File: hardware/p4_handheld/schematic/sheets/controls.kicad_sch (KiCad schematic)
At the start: 0 parts

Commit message: hw(p4_handheld): controls sheet, 11 direct-GPIO buttons off strap pins
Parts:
- added SW1: NavSwitch-Up, SW-SMD_4P-L4.5-W4.5-P3.00-LS4.5-TL, symbol Switch:SW_Push
- added SW10A: Btn-VolUp, SW-SMD_2P-L3.9-W2.9-P1.90-LS2.8-BR, symbol Switch:SW_Push
- added SW10B: Btn-VolDown, SW-SMD_2P-L3.9-W2.9-P1.90-LS2.8-BR, symbol Switch:SW_Push
- added SW11: NavSwitch-Center, SW-SMD_4P-L4.5-W4.5-P3.00-LS4.5-TL, symbol Switch:SW_Push
- added SW2: NavSwitch-Down, SW-SMD_4P-L4.5-W4.5-P3.00-LS4.5-TL, symbol Switch:SW_Push
- added SW3: NavSwitch-Left, SW-SMD_4P-L4.5-W4.5-P3.00-LS4.5-TL, symbol Switch:SW_Push
- added SW4: NavSwitch-Right, SW-SMD_4P-L4.5-W4.5-P3.00-LS4.5-TL, symbol Switch:SW_Push
- added SW5: Btn-Undo, SW-SMD_4P-L6.0-W6.0-P4.50-LS6.5-TL, symbol Switch:SW_Push
- added SW6: Btn-Action, SW-SMD_4P-L6.0-W6.0-P4.50-LS6.5-TL, symbol Switch:SW_Push
- added SW7: Btn-Restart, SW-SMD_4P-L6.0-W6.0-P4.50-LS6.5-TL, symbol Switch:SW_Push
- added SW8: Btn-Menu, SW-SMD_4P-L6.0-W6.0-P4.50-LS6.5-TL, symbol Switch:SW_Push

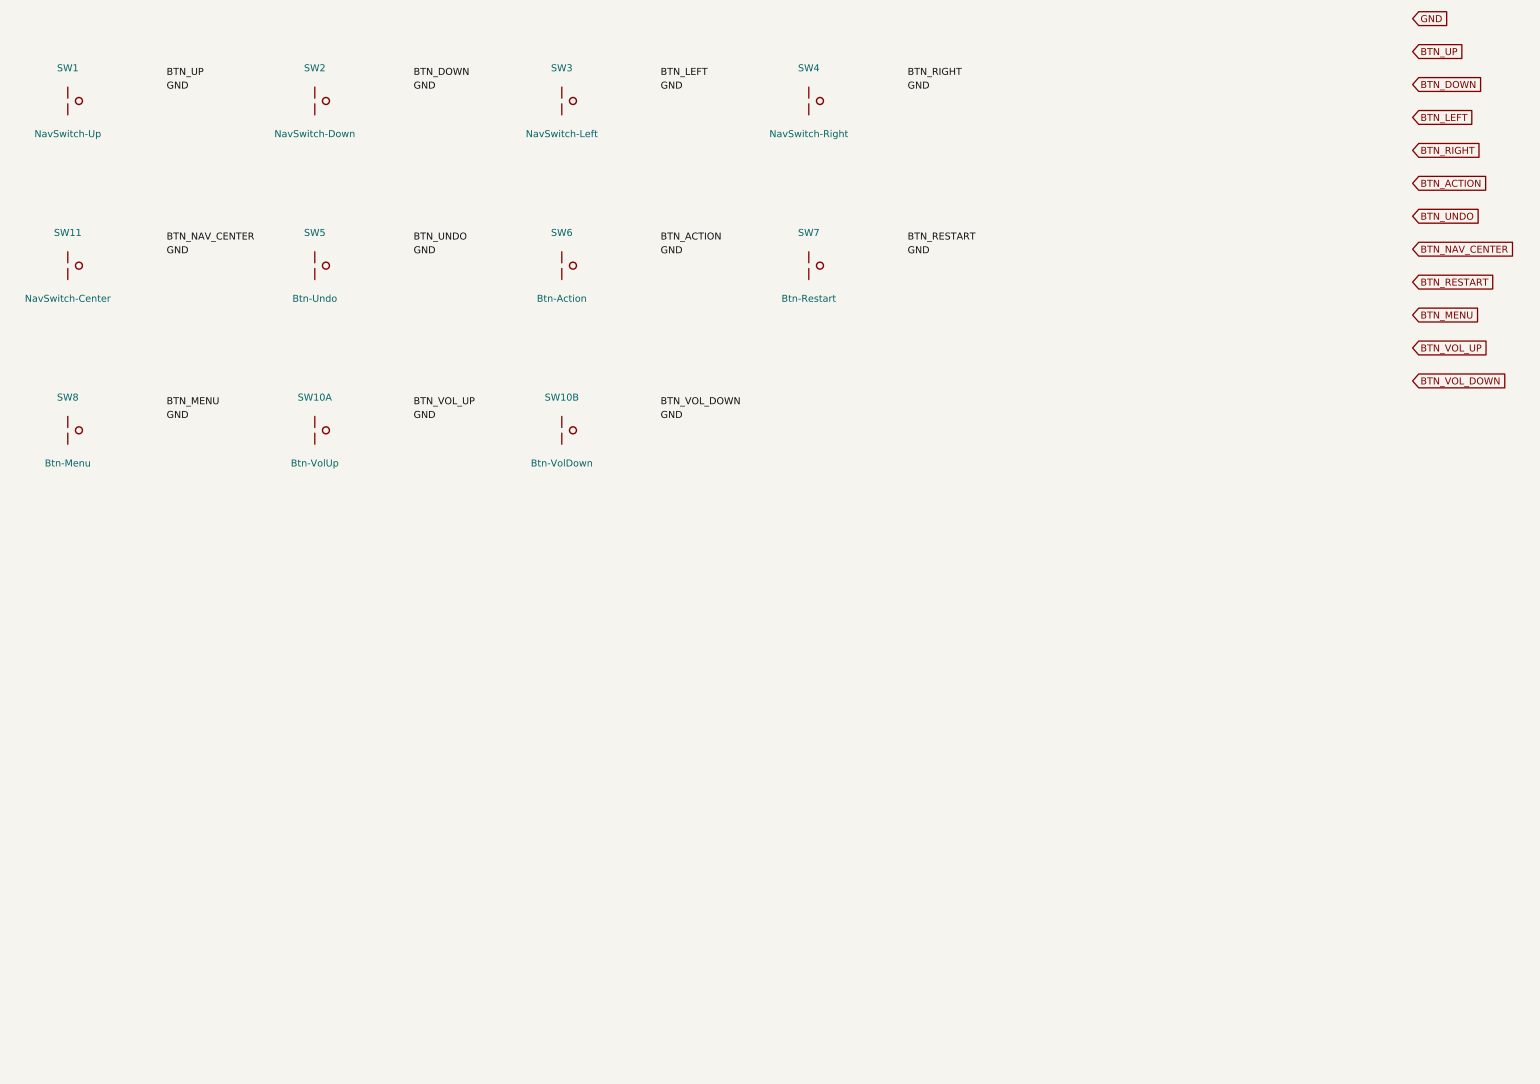
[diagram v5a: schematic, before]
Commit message: hw(p4_handheld): ERC-clean schematic engine (real pins, on-endpoint labels, project symbol lib)
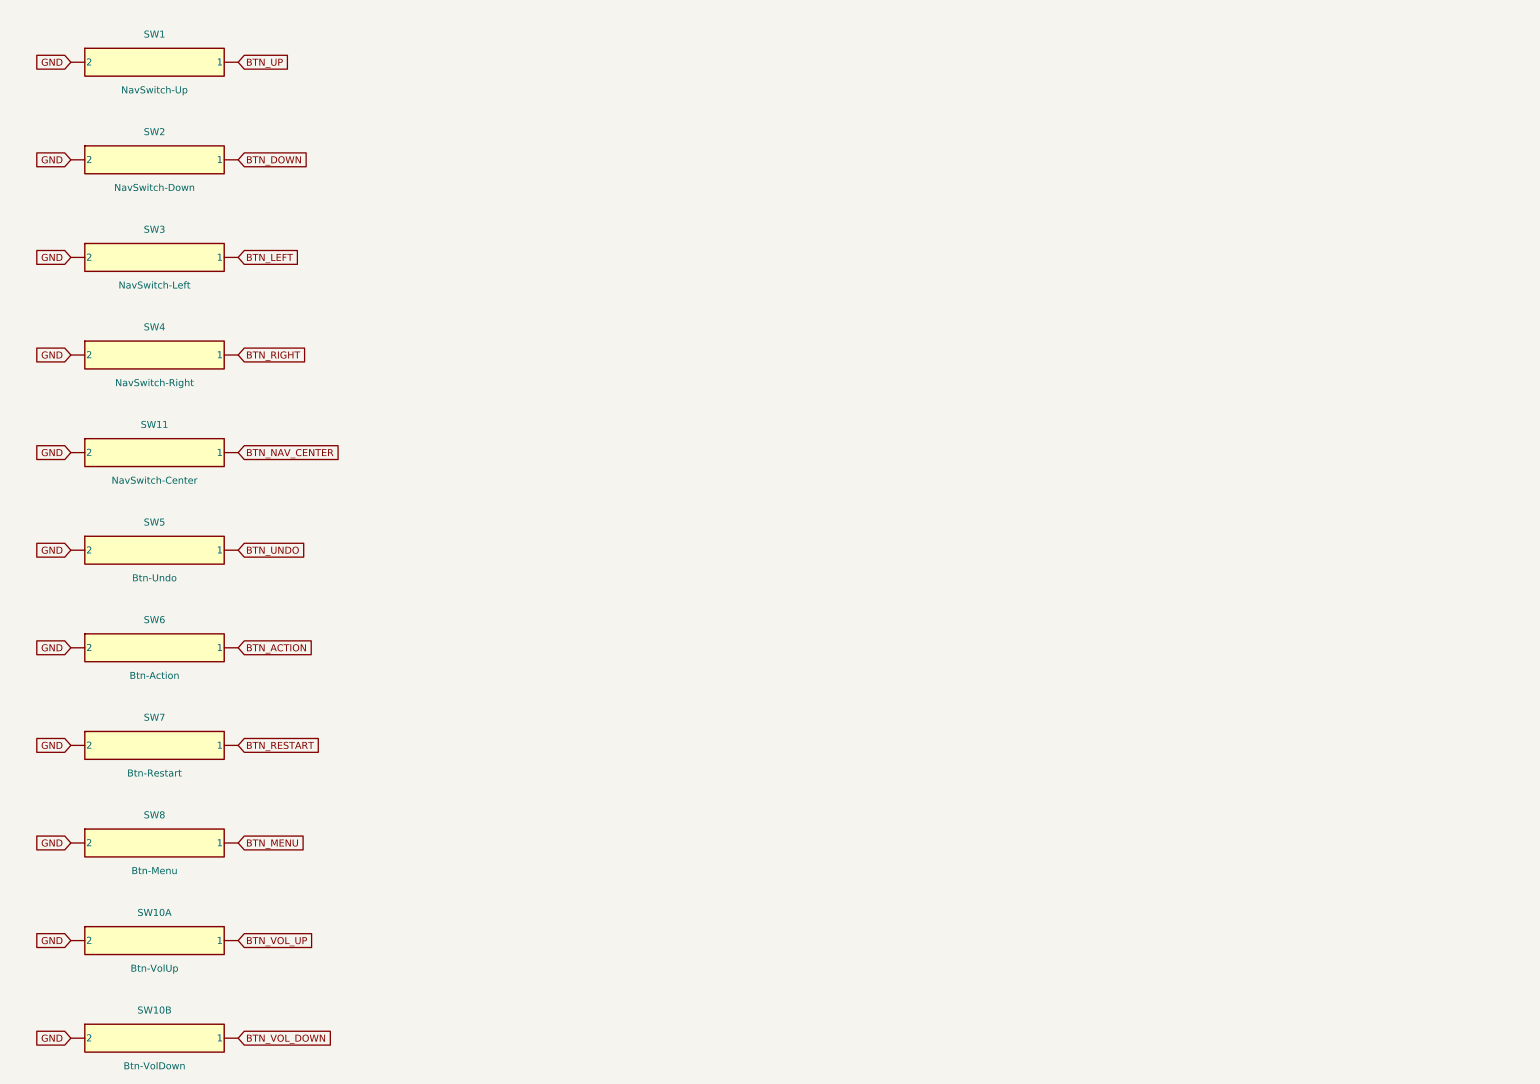
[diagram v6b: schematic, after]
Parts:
- removed SW1: NavSwitch-Up, SW-SMD_4P-L4.5-W4.5-P3.00-LS4.5-TL, symbol Switch:SW_Push
- removed SW10A: Btn-VolUp, SW-SMD_2P-L3.9-W2.9-P1.90-LS2.8-BR, symbol Switch:SW_Push
- removed SW10B: Btn-VolDown, SW-SMD_2P-L3.9-W2.9-P1.90-LS2.8-BR, symbol Switch:SW_Push
- removed SW11: NavSwitch-Center, SW-SMD_4P-L4.5-W4.5-P3.00-LS4.5-TL, symbol Switch:SW_Push
- removed SW2: NavSwitch-Down, SW-SMD_4P-L4.5-W4.5-P3.00-LS4.5-TL, symbol Switch:SW_Push
- removed SW3: NavSwitch-Left, SW-SMD_4P-L4.5-W4.5-P3.00-LS4.5-TL, symbol Switch:SW_Push
- removed SW4: NavSwitch-Right, SW-SMD_4P-L4.5-W4.5-P3.00-LS4.5-TL, symbol Switch:SW_Push
- removed SW5: Btn-Undo, SW-SMD_4P-L6.0-W6.0-P4.50-LS6.5-TL, symbol Switch:SW_Push
- removed SW6: Btn-Action, SW-SMD_4P-L6.0-W6.0-P4.50-LS6.5-TL, symbol Switch:SW_Push
- removed SW7: Btn-Restart, SW-SMD_4P-L6.0-W6.0-P4.50-LS6.5-TL, symbol Switch:SW_Push
- removed SW8: Btn-Menu, SW-SMD_4P-L6.0-W6.0-P4.50-LS6.5-TL, symbol Switch:SW_Push
- added SW1: NavSwitch-Up, symbol PSP4H:SYM_SW1
- added SW10A: Btn-VolUp, symbol PSP4H:SYM_SW10A
- added SW10B: Btn-VolDown, symbol PSP4H:SYM_SW10B
- added SW11: NavSwitch-Center, symbol PSP4H:SYM_SW11
- added SW2: NavSwitch-Down, symbol PSP4H:SYM_SW2
- added SW3: NavSwitch-Left, symbol PSP4H:SYM_SW3
- added SW4: NavSwitch-Right, symbol PSP4H:SYM_SW4
- added SW5: Btn-Undo, symbol PSP4H:SYM_SW5
- added SW6: Btn-Action, symbol PSP4H:SYM_SW6
- added SW7: Btn-Restart, symbol PSP4H:SYM_SW7
- added SW8: Btn-Menu, symbol PSP4H:SYM_SW8
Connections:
- net BTN_ACTION: now also SW6.1
- net BTN_DOWN: now also SW2.1
- net BTN_LEFT: now also SW3.1
- net BTN_MENU: now also SW8.1
- net BTN_NAV_CENTER: now also SW11.1
- net BTN_RESTART: now also SW7.1
- net BTN_RIGHT: now also SW4.1
- net BTN_UNDO: now also SW5.1
- net BTN_UP: now also SW1.1
- net BTN_VOL_DOWN: now also SW10B.1
- net BTN_VOL_UP: now also SW10A.1
- net GND: now also SW1.2, SW10A.2, SW10B.2, SW11.2, SW2.2, SW3.2, SW4.2, SW5.2, SW6.2, SW7.2, SW8.2
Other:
- title: PuzzleScript Card — controls -> PuzzleScript P4 Handheld — controls
